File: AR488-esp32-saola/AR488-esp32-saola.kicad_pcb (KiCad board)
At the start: 2 copper layers, 63.5 x 40.6 mm, 2 parts, among them J2 Conn_02x12_Odd_Even, U1 ESP32-S2-Saola-1

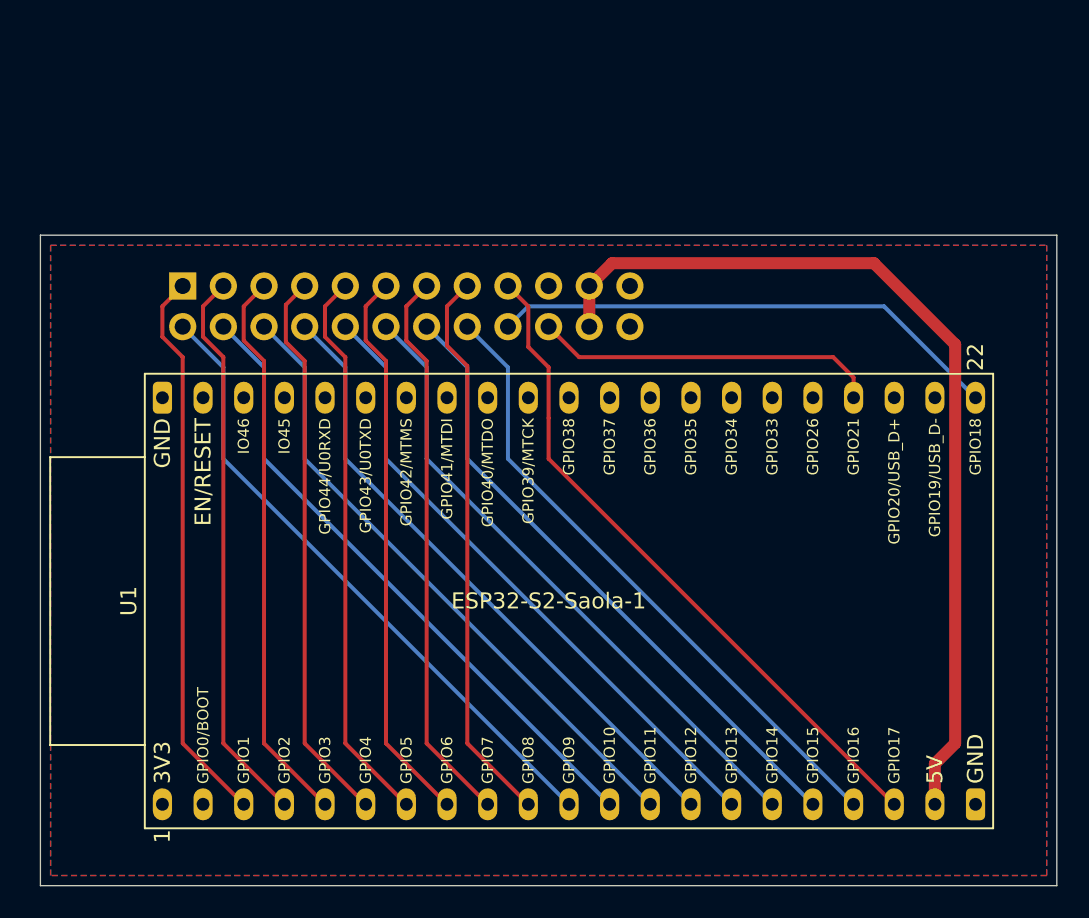
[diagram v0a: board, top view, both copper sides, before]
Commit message: Better pin assignment for the inter-PCB connector
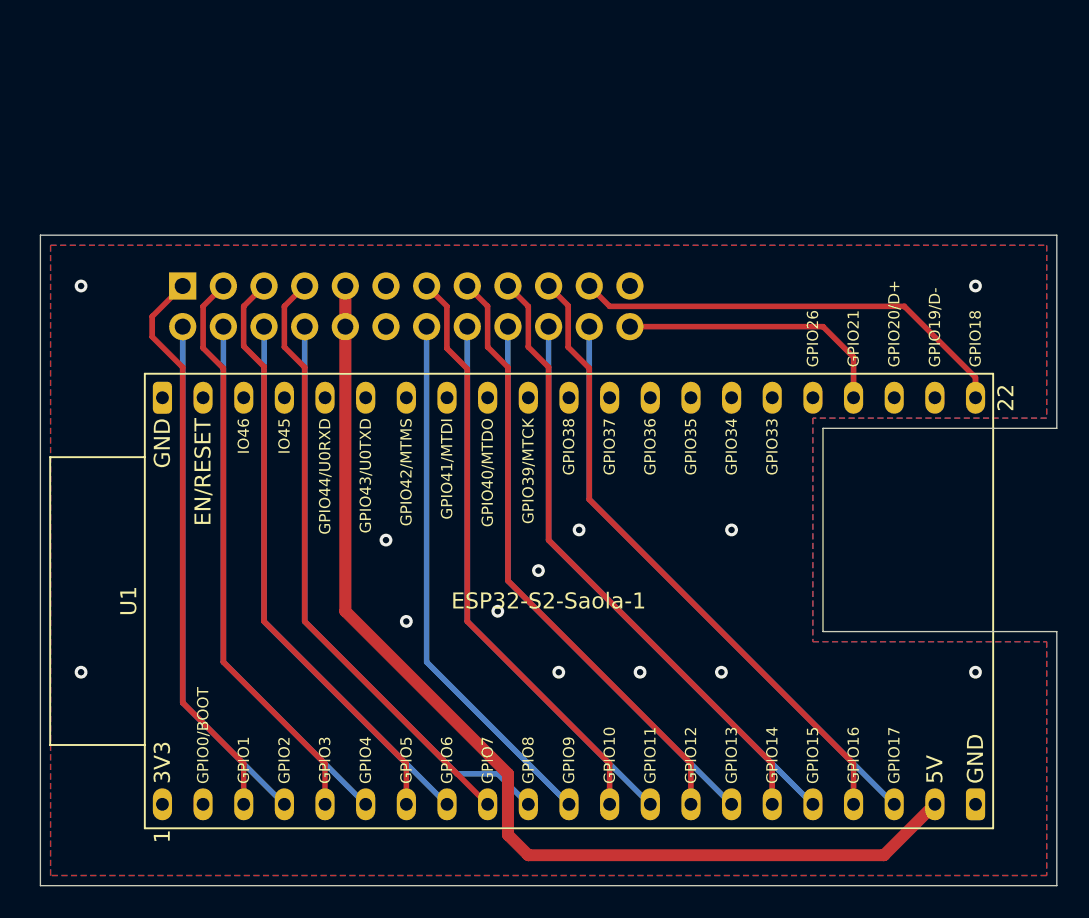
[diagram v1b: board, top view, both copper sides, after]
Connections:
- J2 pad 10: DAV_a -> +5V
- J2 pad 11: D6 -> GND
- J2 pad 12: EOI_a -> GND
- J2 pad 13: D7 -> IFC_a
- J2 pad 14: ATN_a -> REN_a
- J2 pad 15: D8 -> NRFD_a
- J2 pad 16: SRQ_a -> NDAC_a
- J2 pad 17: TE -> EOI_a
- J2 pad 18: SC -> DAV_a
- J2 pad 19: GND -> SRQ_a
- J2 pad 2: REN_a -> D2
- J2 pad 20: DC -> ATN_a
- J2 pad 21: +5V -> SC
- J2 pad 22: +5V -> TE
- J2 pad 24: GND -> DC
- J2 pad 3: D2 -> D3
- J2 pad 4: IFC_a -> D4
- J2 pad 5: D3 -> D5
- J2 pad 6: NDAC_a -> D6
- J2 pad 7: D4 -> D7
- J2 pad 8: NRFD_a -> D8
- J2 pad 9: D5 -> +5V
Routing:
- net +5V: track 57.4 -> 67.0 mm
- net REN_a: track 39.8 -> 33.5 mm
- net NDAC_a: track 39.8 -> 34.6 mm
- net TE: track 42.4 -> 37.7 mm
- net SC: track 32.1 -> 27.8 mm
- net DC: track 21.6 -> 17.3 mm
- net DAV_a: track 39.8 -> 35.6 mm
- net D7: track 35.0 -> 38.2 mm
- net ATN_a: track 39.8 -> 36.7 mm
- net IFC_a: track 39.8 -> 37.1 mm
- net D2: track 35.0 -> 32.5 mm
- net D8: track 35.0 -> 37.1 mm
- net D5: track 35.0 -> 37.1 mm
- net NRFD_a: track 39.8 -> 38.2 mm
- net D4: track 34.9 -> 33.5 mm
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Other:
- outline, holes or cut-outs redrawn

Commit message: Finish the commons board + esp32 s2 soala + esp32 devkitc boards
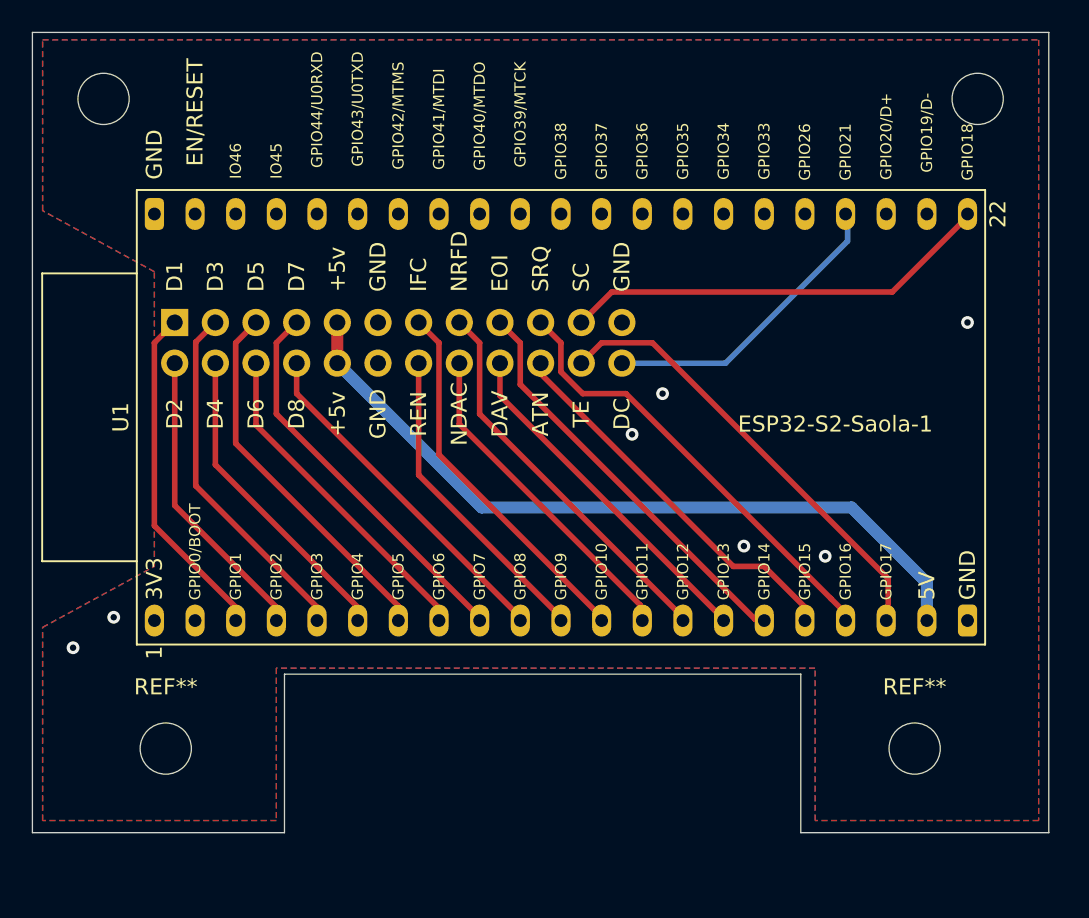
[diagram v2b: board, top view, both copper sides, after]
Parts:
- added REF**: OSHW-Logo2_7.3x6mm_SilkScreen, Symbol:OSHW-Logo2_7.3x6mm_SilkScreen, B.Cu at (119.5, 91.8)
- added REF**: MountingHole_3.2mm_M3_ISO7380, MountingHole:MountingHole_3.2mm_M3_ISO7380, F.Cu at (122.1, 67.7)
- added REF**: MountingHole_3.2mm_M3_ISO7380, MountingHole:MountingHole_3.2mm_M3_ISO7380, F.Cu at (67.4, 67.7)
- added REF**: MountingHole_3.2mm_M3_ISO7380, MountingHole:MountingHole_3.2mm_M3_ISO7380, F.Cu at (118.1, 108.3)
- added REF**: MountingHole_3.2mm_M3_ISO7380, MountingHole:MountingHole_3.2mm_M3_ISO7380, F.Cu at (71.3, 108.3)
- moved U1 11.5 mm to (70.6, 100.3)
- moved J2 2.33 mm to (71.9, 81.7)
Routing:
- net +5V: track 67.0 -> 47.6 mm
- net D8: track 37.1 -> 22.0 mm
- net NRFD_a: track 38.2 -> 24.2 mm
- net NDAC_a: track 34.6 -> 20.7 mm
- net D3: track 36.1 -> 22.2 mm
- net D1: track 35.5 -> 21.7 mm
- net IFC_a: track 37.1 -> 23.3 mm
- net DAV_a: track 35.6 -> 21.8 mm
- net D7: track 38.2 -> 24.4 mm
- net D6: track 34.6 -> 20.8 mm
- net D2: track 32.5 -> 18.7 mm
- net D5: track 37.1 -> 23.4 mm
- net D4: track 33.5 -> 19.9 mm
- net REN_a: track 33.5 -> 19.9 mm
- net EOI_a: track 39.2 -> 25.7 mm
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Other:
- board size 63.5 x 40.6 mm -> 63.5 x 50 mm
- board text added: "+5v"
- board text added: "AR488-GPIB ESP32-S2-Soala adapter"
- board text added: "ATN"
- board text added: "CC BY-SA 3.0 David Douard <david.douard@sdfa3.org>"
- board text added: "D1"
- board text added: "D2"
- board text added: "D3"
- board text added: "D4"
- board text added: "D5"
- board text added: "D6"
- board text added: "D7"
- board text added: "D8"
- board text added: "DAV"
- board text added: "DC"
- board text added: "EOI"
- board text added: "GND"
- board text added: "IFC"
- board text added: "NDAC"
- board text added: "NRFD"
- board text added: "REN"
- board text added: "SC"
- board text added: "SRQ"
- board text added: "TE"
- board text added: "https://whatever.sdfa3.org/gpib"

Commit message: Several minor fixes and adjustments in PCBs
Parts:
- moved REF** 2.70 mm to (121.0, 89.6)
- moved REF** 0.06 mm to (71.4, 108.2)
- moved REF** 0.06 mm to (118.2, 108.2)
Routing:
- net GND: vias 7 -> 23
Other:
- board text added: "AR488-GPIB ESP32-S2-Saola adapter"
- board text removed: "AR488-GPIB ESP32-S2-Soala adapter"
